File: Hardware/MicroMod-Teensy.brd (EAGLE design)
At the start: 22 x 22.8 mm, 80 parts, among them J1 MICROMOD-2222, Q1 20V/4.2A/52mΩ/1.4W, Q2 20V/0.2A/8MHz/1.2Ω/1Vth, U1 IMXRT1062DV10X10, U3 MKL02Z32VFG4, U4 W25QXX128MBIT-6X5, Y1 32.768kHz, Y2 24MHz

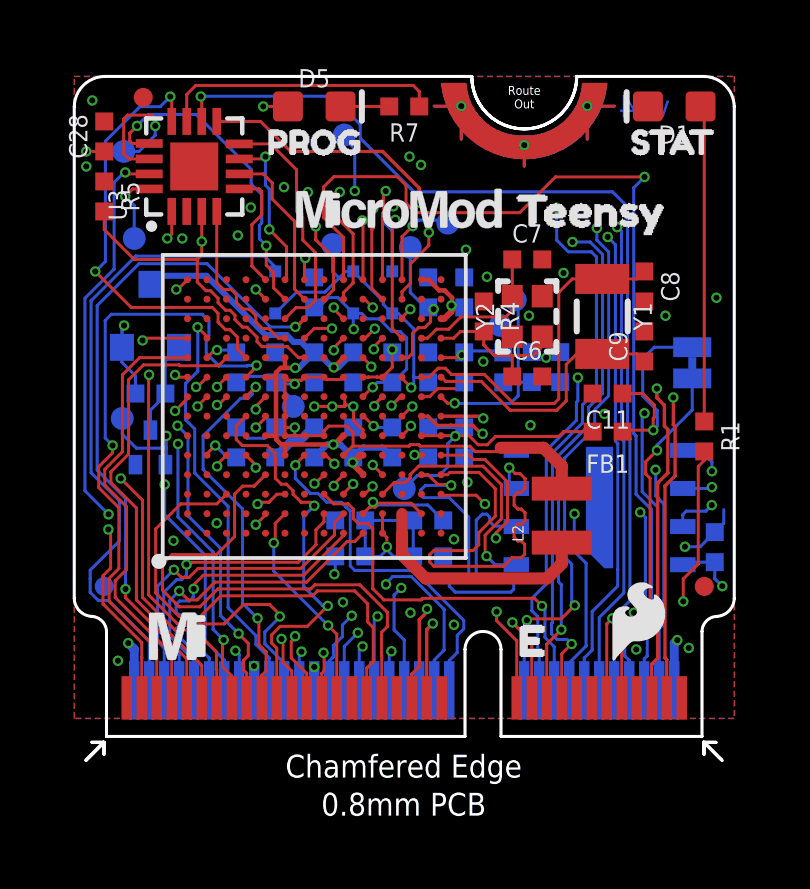
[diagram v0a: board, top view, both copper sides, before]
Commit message: Moved test-points for ideal testing
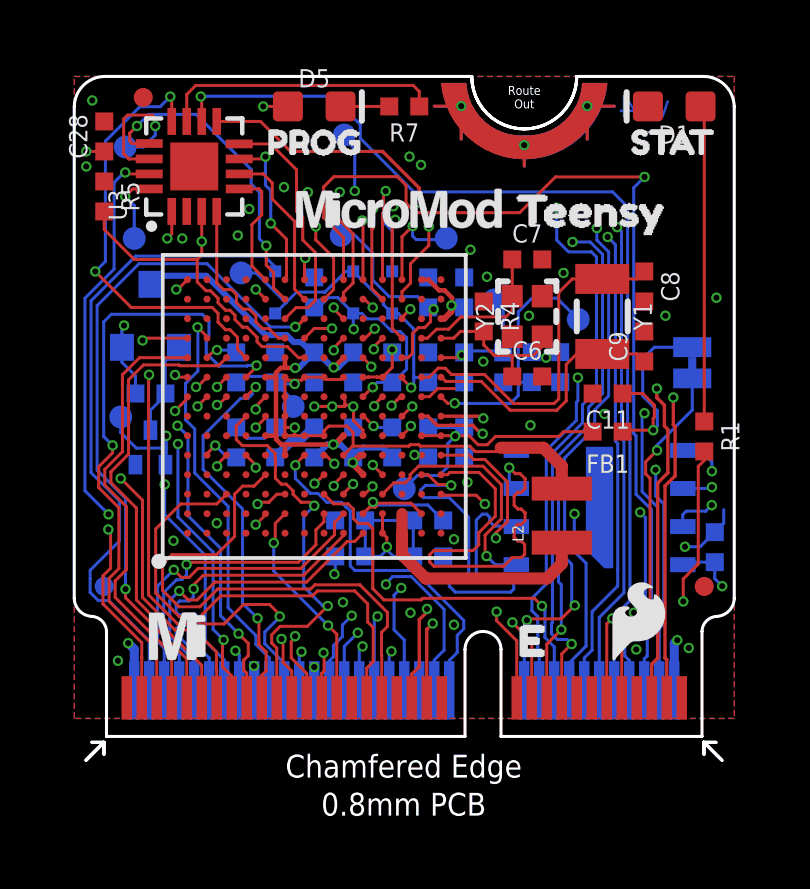
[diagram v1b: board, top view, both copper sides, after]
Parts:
- moved TP4 3.19 mm to (5.56, 15.4)
- moved TP5 2.33 mm to (8.90, 16.7)
- moved TP7 2.20 mm to (16.8, 13.9)
- moved TP6 0.87 mm to (14.0, 14.5)
- moved TP1 0.50 mm to (12.4, 16.6)
- moved TP9 0.16 mm to (1.70, 19.6)
- moved TP2 0.07 mm to (1.55, 10.6)
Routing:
- net VDD_SNVS_CAP: track 4.81 -> 7.02 mm
- net VDD_HIGH_CAP: track 7.41 -> 9.45 mm
- net NVCC_PLL: track 3.14 -> 4.07 mm
- net VDD_SNVS_IN: track 10.4 -> 11.1 mm

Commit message: Connect 3.3V_Controlled to peripherals. Increase internal power trace widths.
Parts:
- added TP12, TP13: (no value), SparkFun-Connectors:PAD.03X.03
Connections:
- net N$3 renamed DCDC_IN
- net N$9 renamed DCDC_LP
- net 3.3V: now also TP13.P$1; no longer C28.1, C29.1, D5.A, FB2.1, U3.1, U4.8
- net 3.3V_CONTROLLED: now also C28.1, C29.1, D5.A, FB2.1, TP12.P$1, U3.1, U4.8
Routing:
- net 3.3V_CONTROLLED: track 28.8 -> 86.3 mm, vias 5 -> 12
- net JTAG_TRST: track 31.4 -> 36.4 mm
- net PROGRAM: track 33.6 -> 34.8 mm, vias 2 -> 3
- net 3.3V: track 13.2 -> 12.1 mm, vias 9 -> 4
- net N$10: track 7.55 -> 6.73 mm
- net SDA/18/A4: track 33.8 -> 34.3 mm

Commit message: moved some TP's around to get clearence for pogopins
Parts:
- moved TP9 2.04 mm to (3.74, 19.5)
- moved TP11 1.86 mm to (7.14, 20.1)
- moved TP13 0.77 mm to (10.8, 21.1)
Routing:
- net VDD_USB_CAP: track 13.9 -> 15.7 mm
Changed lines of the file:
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@@
 <?xml version="1.0" encoding="utf-8"?>
 <!DOCTYPE eagle SYSTEM "eagle.dtd">
-<eagle version="9.6.0">
+<eagle version="9.5.0">
 <drawing>
 <settings>
-<setting alwaysvectorfont="yes"/>
+<setting alwaysvectorfont="no"/>
 <setting verticaltext="up"/>
 </settings>
 <grid distance="1" unitdist="mm" unit="mm" style="lines" multiple="1" display="yes" altdistance="0.025" altunitdist="mm" altunit="mm"/>
 <layers>
-<layer number="1" name="Top" color="4" fill="1" visible="no" active="yes"/>
+<layer number="1" name="Top" color="4" fill="1" visible="yes" active="yes"/>
 <layer number="2" name="Vert-GND" color="1" fill="3" visible="no" active="yes"/>
 <layer number="15" name="Horz-3V3" color="4" fill="6" visible="no" active="yes"/>
@@
 <layer number="19" name="Unrouted" color="6" fill="1" visible="yes" active="yes"/>
 <layer number="20" name="Dimension" color="24" fill="1" visible="yes" active="yes"/>
-<layer number="21" name="tPlace" color="16" fill="1" visible="no" active="yes"/>
-<layer number="22" name="bPlace" color="14" fill="1" visible="no" active="yes"/>
-<layer number="23" name="tOrigins" color="15" fill="1" visible="no" active="yes"/>
+<layer number="21" name="tPlace" color="16" fill="1" visible="yes" active="yes"/>
+<layer number="22" name="bPlace" color="14" fill="1" visible="yes" active="yes"/>
+<layer number="23" name="tOrigins" color="15" fill="1" visible="yes" active="yes"/>
 <layer number="24" name="bOrigins" color="15" fill="1" visible="yes" active="yes"/>
 <layer number="25" name="tNames" color="7" fill="1" visible="no" active="yes"/>
@@
 <layer number="43" name="vRestrict" color="2" fill="10" visible="no" active="yes"/>
 <layer number="44" name="Drills" color="7" fill="1" visible="no" active="yes"/>
-<layer number="45" name="Holes" color="7" fill="1" visible="no" active="yes"/>
+<layer number="45" name="Holes" color="7" fill="1" visible="yes" active="yes"/>
 <layer number="46" name="Milling" color="3" fill="1" visible="no" active="yes"/>
 <layer number="47" name="Measures" color="7" fill="1" visible="no" active="yes"/>
 <layer number="48" name="Document" color="7" fill="1" visible="no" active="yes"/>
-<layer number="49" name="Reference" color="7" fill="1" visible="no" active="yes"/>
+<layer number="49" name="Reference" color="7" fill="1" visible="yes" active="yes"/>
 <layer number="50" name="dxf" color="7" fill="1" visible="no" active="yes"/>
-<layer number="51" name="tDocu" color="6" fill="1" visible="no" active="yes"/>
+<layer number="51" name="tDocu" color="6" fill="1" visible="yes" active="yes"/>
 <layer number="52" name="bDocu" color="7" fill="1" visible="no" active="yes"/>
 <layer number="91" name="Nets" color="2" fill="1" visible="no" active="no"/>
@@
 </element>
 <element name="TP8" library="SparkFun-Connectors" package="PAD.03X.03" value="" x="2" y="16.59" smashed="yes" rot="MR0"/>
-<element name="TP9" library="SparkFun-Connectors" package="PAD.03X.03" value="" x="1.7" y="19.64" smashed="yes" rot="MR0"/>
+<element name="TP9" library="SparkFun-Connectors" package="PAD.03X.03" value="" x="3.736" y="19.487" smashed="yes" rot="MR0"/>
 <element name="C28" library="SparkFun-Capacitors" package="0402-TIGHT" value="0.22uF" x="1" y="19.99" smashed="yes" rot="R90">
 <attribute name="NAME" x="0.438" y="19.99" size="0.6096" layer="25" font="vector" ratio="20" rot="R90" align="bottom-center"/>
@@
 </element>
 <element name="TP10" library="SparkFun-Connectors" package="PAD.03X.03" value="" x="7.3" y="10.99" smashed="yes" rot="MR270"/>
-<element name="TP11" library="SparkFun-Connectors" package="PAD.03X.03" value="" x="9" y="20.04" smashed="yes" rot="MR270"/>
+<element name="TP11" library="SparkFun-Connectors" package="PAD.03X.03" value="" x="7.137" y="20.122" smashed="yes" rot="MR270"/>
 <element name="U$3" library="buzzard_labels (1)" package="TEENSY2" value="" x="13.858" y="17.516" smashed="yes"/>
 <element name="L2" library="SparkFun-Coils" package="1008(2520)" value="4.7μH" x="16.25" y="7.35" smashed="yes" rot="R90">
@@
 <element name="U$11" library="SparkFun-MicroMod" package="MICROMOD_LOGO_.3" value="" x="16.383" y="17.272" smashed="yes" rot="MR0"/>
 <element name="TP12" library="SparkFun-Connectors" package="PAD.03X.03" value="" x="1.44" y="21.28" smashed="yes" rot="MR0"/>
-<element name="TP13" library="SparkFun-Connectors" package="PAD.03X.03" value="" x="10" y="21" smashed="yes" rot="MR0"/>
+<element name="TP13" library="SparkFun-Connectors" package="PAD.03X.03" value="" x="10.756" y="21.135" smashed="yes" rot="MR0"/>
 </elements>
 <signals>
@@
 <wire x1="10.7605125" y1="17.76395625" x2="10.65965625" y2="17.6631" width="0.2032" layer="16"/>
 <wire x1="10.63535" y1="17.6631" x2="10.65965625" y2="17.6631" width="0.2032" layer="16"/>
-<wire x1="10.7605125" y1="20.2394875" x2="10" y2="21" width="0.2032" layer="16"/>
-<wire x1="10.7605125" y1="17.76395625" x2="10.7605125" y2="20.2394875" width="0.2032" layer="16"/>
+<wire x1="10.7605125" y1="21.1304875" x2="10.756" y2="21.135" width="0.2032" layer="16"/>
+<wire x1="10.7605125" y1="17.76395625" x2="10.7605125" y2="21.1304875" width="0.2032" layer="16"/>
 </signal>
 <signal name="USB_D+" class="1">
@@
 <wire x1="9.2714" y1="18.09235" x2="9.35" y2="18.17095" width="0.1016" layer="2"/>
 <wire x1="9.35" y1="18.17095" x2="9.35" y2="19.57095" width="0.1016" layer="16"/>
-<wire x1="9.35" y1="19.57095" x2="9" y2="19.92095" width="0.1016" layer="16"/>
-<wire x1="9" y1="20.04" x2="9" y2="19.92095" width="0.1016" layer="16"/>
+<wire x1="9.35" y1="19.57095" x2="8.79895" y2="20.122" width="0.1016" layer="16"/>
+<wire x1="7.137" y1="20.122" x2="8.79895" y2="20.122" width="0.1016" layer="16"/>
 </signal>
 <signal name="VDD_SNVS_IN">
@@
 <wire x1="2.5" y1="19.24" x2="1.823" y2="19.24" width="0.1016" layer="1"/>
 <via x="2.7" y="20.34" extent="1-16" drill="0.2"/>
-<wire x1="2.7" y1="20.032" x2="2.308" y2="19.64" width="0.1016" layer="16"/>
-<wire x1="1.7" y1="19.64" x2="2.308" y2="19.64" width="0.1016" layer="16"/>
-<wire x1="2.7" y1="20.34" x2="2.7" y2="20.032" width="0.1016" layer="16"/>
+<wire x1="3.736" y1="19.487" x2="3.561" y2="19.487" width="0.1016" layer="16"/>
+<wire x1="3.561" y1="19.487" x2="2.7" y2="20.348" width="0.1016" layer="16"/>
+<wire x1="2.7" y1="20.348" x2="2.7" y2="20.34" width="0.1016" layer="16"/>
 <via x="14.605" y="3.7913" extent="1-16" drill="0.2"/>
 <via x="11.176" y="19.31865" extent="1-16" drill="0.2"/>

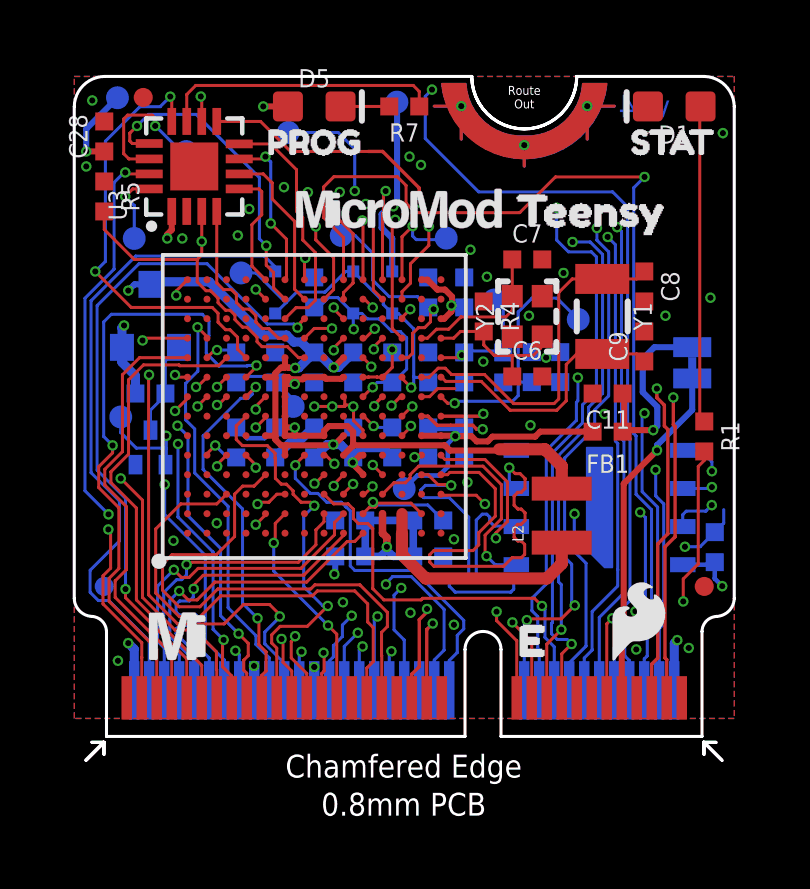
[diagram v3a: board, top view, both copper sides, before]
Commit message: DFM changes: move traces to avoid t/b stop exposure
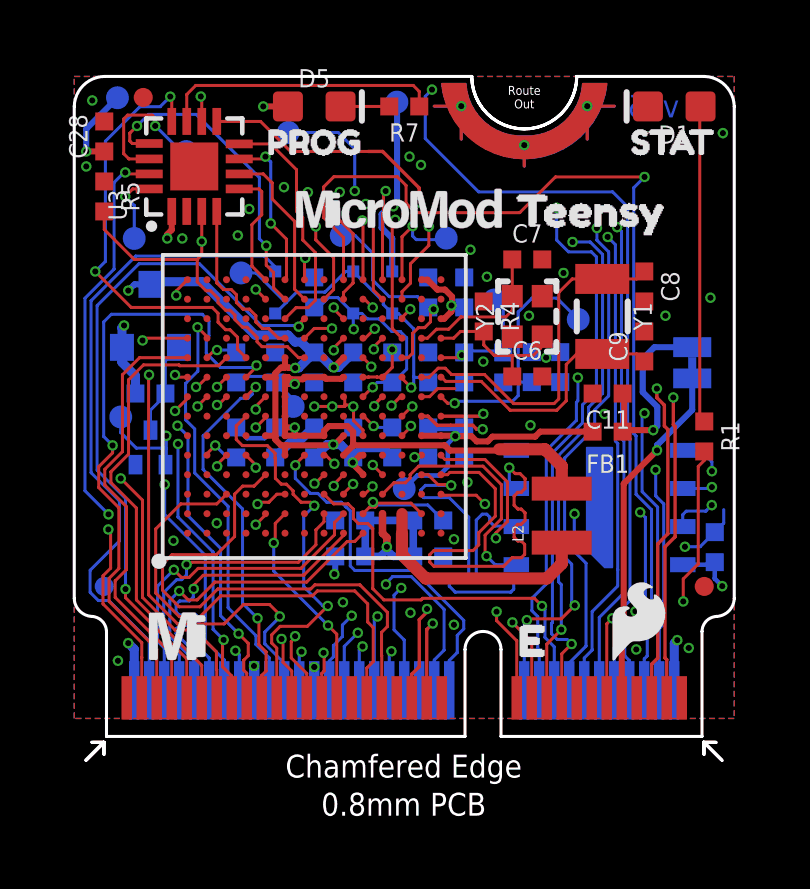
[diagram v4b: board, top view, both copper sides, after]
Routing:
- net GND: track 21.4 -> 20.1 mm
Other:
- board text added: "v15"
- board text removed: "v14"
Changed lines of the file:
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@@
 <?xml version="1.0" encoding="utf-8"?>
 <!DOCTYPE eagle SYSTEM "eagle.dtd">
-<eagle version="9.5.0">
+<eagle version="9.6.0">
 <drawing>
 <settings>
-<setting alwaysvectorfont="no"/>
+<setting alwaysvectorfont="yes"/>
 <setting verticaltext="up"/>
 </settings>
-<grid distance="1" unitdist="mm" unit="mm" style="lines" multiple="1" display="yes" altdistance="0.025" altunitdist="mm" altunit="mm"/>
+<grid distance="1" unitdist="mm" unit="mm" style="lines" multiple="1" display="yes" altdistance="0.1" altunitdist="mm" altunit="mm"/>
 <layers>
 <layer number="1" name="Top" color="4" fill="1" visible="yes" active="yes"/>
@@
 <wire x1="22" y1="18.99" x2="0" y2="18.99" width="0.1016" layer="51"/>
 <wire x1="0" y1="18.99" x2="0" y2="4.99" width="0.1016" layer="51"/>
-<text x="19" y="21" size="0.75" layer="16" font="vector" ratio="20" rot="MR0" align="center">v14</text>
+<text x="19.3" y="21" size="0.75" layer="16" font="vector" ratio="20" rot="MR0" align="center">v15</text>
 <text x="30.35" y="31.67" size="1.778" layer="51" font="vector" ratio="15">0.8mm PCB
 45 degree chamfered edge
@@
 <wire x1="0.815" y1="8.97933125" x2="1.2782" y2="9.44253125" width="0.1016" layer="1"/>
 <wire x1="1.2782" y1="9.44253125" x2="1.2782" y2="9.69" width="0.1016" layer="1"/>
-<wire x1="6.0751" y1="12.35546875" x2="5.78099375" y2="12.35546875" width="0.1016" layer="16"/>
-<wire x1="5.78099375" y1="12.35546875" x2="5.763125" y2="12.3376" width="0.1016" layer="16"/>
 <wire x1="0.98125" y1="13.80591875" x2="0.98125" y2="9.98695" width="0.1016" layer="16"/>
 <wire x1="1.2782" y1="9.69" x2="0.98125" y2="9.98695" width="0.1016" layer="16"/>
@@
 <contactref element="J1" pad="71"/>
 <wire x1="2.75" y1="1.275" x2="2.75" y2="2.90303125" width="0.1016" layer="1"/>
-<wire x1="4.8276875" y1="12.3376" x2="4.4" y2="12.7652875" width="0.1016" layer="16"/>
 <wire x1="4.4" y1="13.2552875" x2="4.49" y2="13.3452875" width="0.1016" layer="16"/>
 <wire x1="4.49" y1="13.3452875" x2="4.49" y2="13.83864375" width="0.1016" layer="16"/>
-<wire x1="5.763125" y1="12.3376" x2="4.8276875" y2="12.3376" width="0.1016" layer="16"/>
 <wire x1="4.4" y1="12.7652875" x2="4.4" y2="13.2552875" width="0.1016" layer="16"/>
+<wire x1="6.0751" y1="12.35546875" x2="6.0751" y2="12.349575" width="0.1016" layer="16"/>
+<wire x1="6.0751" y1="12.349575" x2="6.013125" y2="12.2876" width="0.1016" layer="16"/>
+<wire x1="6.013125" y1="12.2876" x2="4.8776875" y2="12.2876" width="0.1016" layer="16"/>
+<wire x1="4.8776875" y1="12.2876" x2="4.4" y2="12.7652875" width="0.1016" layer="16"/>
 </signal>
 <signal name="D1/5">
@@
 <signal name="GPIO/26/A12">
 <contactref element="U1" pad="G12"/>
-<wire x1="7.675" y1="13.915" x2="7.4432" y2="13.6832" width="0.1143" layer="1"/>
-<wire x1="7.4432" y1="13.6832" x2="7.4432" y2="13.6184875" width="0.1143" layer="1"/>
-<via x="7.4432" y="13.6184875" extent="1-16" drill="0.2"/>
+<wire x1="7.675" y1="13.915" x2="7.4832" y2="13.7232" width="0.1143" layer="1"/>
+<wire x1="7.4832" y1="13.7232" x2="7.4832" y2="13.6484875" width="0.1143" layer="1"/>
+<via x="7.4832" y="13.6484875" extent="1-16" drill="0.2"/>
 <via x="1.7086" y="4.901" extent="1-16" drill="0.2"/>
 <wire x1="1.7086" y1="7.92063125" x2="1.7086" y2="4.901" width="0.1016" layer="16"/>
@@
 <contactref element="J1" pad="67"/>
 <wire x1="3.75" y1="1.275" x2="3.75" y2="2.57448125" width="0.1016" layer="1"/>
-<wire x1="7.4432" y1="13.6184875" x2="7.3240875" y2="13.7376" width="0.1016" layer="16"/>
-<wire x1="7.3240875" y1="13.7376" x2="6.436875" y2="13.7376" width="0.1016" layer="16"/>
-<wire x1="6.436875" y1="13.7376" x2="4.426475" y2="15.748" width="0.1016" layer="16"/>
-<wire x1="4.426475" y1="15.748" x2="2.159" y2="15.748" width="0.1016" layer="16"/>
+<wire x1="7.4832" y1="13.6484875" x2="7.4440875" y2="13.6876" width="0.1016" layer="16"/>
+<wire x1="7.4440875" y1="13.6876" x2="6.232875" y2="13.6876" width="0.1016" layer="16"/>
+<wire x1="6.232875" y1="13.6876" x2="4.172475" y2="15.748" width="0.1016" layer="16"/>
+<wire x1="4.172475" y1="15.748" x2="2.159" y2="15.748" width="0.1016" layer="16"/>
 <wire x1="2.159" y1="15.748" x2="0.7632" y2="14.3522" width="0.1016" layer="16"/>
 <wire x1="0.7632" y1="14.3522" x2="0.7632" y2="8.86603125" width="0.1016" layer="16"/>
@@
 <wire x1="10.09119375" y1="11.97111875" x2="10.0973125" y2="11.965" width="0.1016" layer="1"/>
 <wire x1="10.0973125" y1="11.965" x2="10.275" y2="11.965" width="0.1016" layer="1"/>
-<wire x1="10.6" y1="12.89" x2="11.85" y2="12.89" width="0.1016" layer="15"/>
 <wire x1="5.4" y1="9.29" x2="5.1" y2="9.29" width="0.1016" layer="16"/>
 <wire x1="5.1" y1="9.29" x2="4.7" y2="9.69" width="0.1016" layer="16"/>
@@
 <wire x1="12.5728875" y1="14.35455625" x2="12.5728875" y2="14.15455625" width="0.2032" layer="1"/>
 <wire x1="12.5728875" y1="14.15455625" x2="12.33333125" y2="13.915" width="0.2032" layer="1"/>
-<wire x1="4.5044" y1="15.1456" x2="2.6256" y2="15.1456" width="0.3048" layer="16"/>
+<wire x1="4.2504" y1="15.1456" x2="2.6256" y2="15.1456" width="0.3048" layer="16"/>
 <wire x1="2.54" y1="15.06" x2="2.6256" y2="15.1456" width="0.2032" layer="16"/>
-<wire x1="4.5044" y1="15.1456" x2="6.2806" y2="13.3694" width="0.3048" layer="16"/>
+<wire x1="4.2504" y1="15.1456" x2="6.0266" y2="13.3694" width="0.3048" layer="16"/>
 <wire x1="9.92920625" y1="13.9592875" x2="10.20143125" y2="13.9592875" width="0.1016" layer="15"/>
 <wire x1="10.20143125" y1="13.9592875" x2="10.36071875" y2="13.8" width="0.1016" layer="15"/>
@@
 <wire x1="9.68671875" y1="13.43945625" x2="9.68671875" y2="13.7168" width="0.1016" layer="15"/>
 <wire x1="9.31905" y1="13.0717875" x2="9.68671875" y2="13.43945625" width="0.1016" layer="15"/>
-<wire x1="7.07873125" y1="13.3694" x2="7.31104375" y2="13.1370875" width="0.3048" layer="16"/>
-<wire x1="7.31104375" y1="13.1370875" x2="7.5639125" y2="13.1370875" width="0.3048" layer="16"/>
+<wire x1="7.12873125" y1="13.3694" x2="7.36104375" y2="13.1370875" width="0.3048" layer="16"/>
+<wire x1="7.36104375" y1="13.1370875" x2="7.5639125" y2="13.1370875" width="0.3048" layer="16"/>
 <wire x1="7.5639125" y1="13.1370875" x2="7.9555" y2="12.7455" width="0.3048" layer="16"/>
-<wire x1="6.2806" y1="13.3694" x2="7.07873125" y2="13.3694" width="0.3048" layer="16"/>
+<wire x1="6.0266" y1="13.3694" x2="7.12873125" y2="13.3694" width="0.3048" layer="16"/>
 <contactref element="U3" pad="1"/>
 <via x="3.1" y="16.59" extent="1-16" drill="0.2"/>
